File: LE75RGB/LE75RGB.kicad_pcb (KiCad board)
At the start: 2 copper layers, 285 x 94.6 mm, 256 parts, among them P1 USB_C_Plug_USB2.0, SW1 SW_Push, U1 MCP1703Ax-330xxDB, U2 STM32F072CBTx

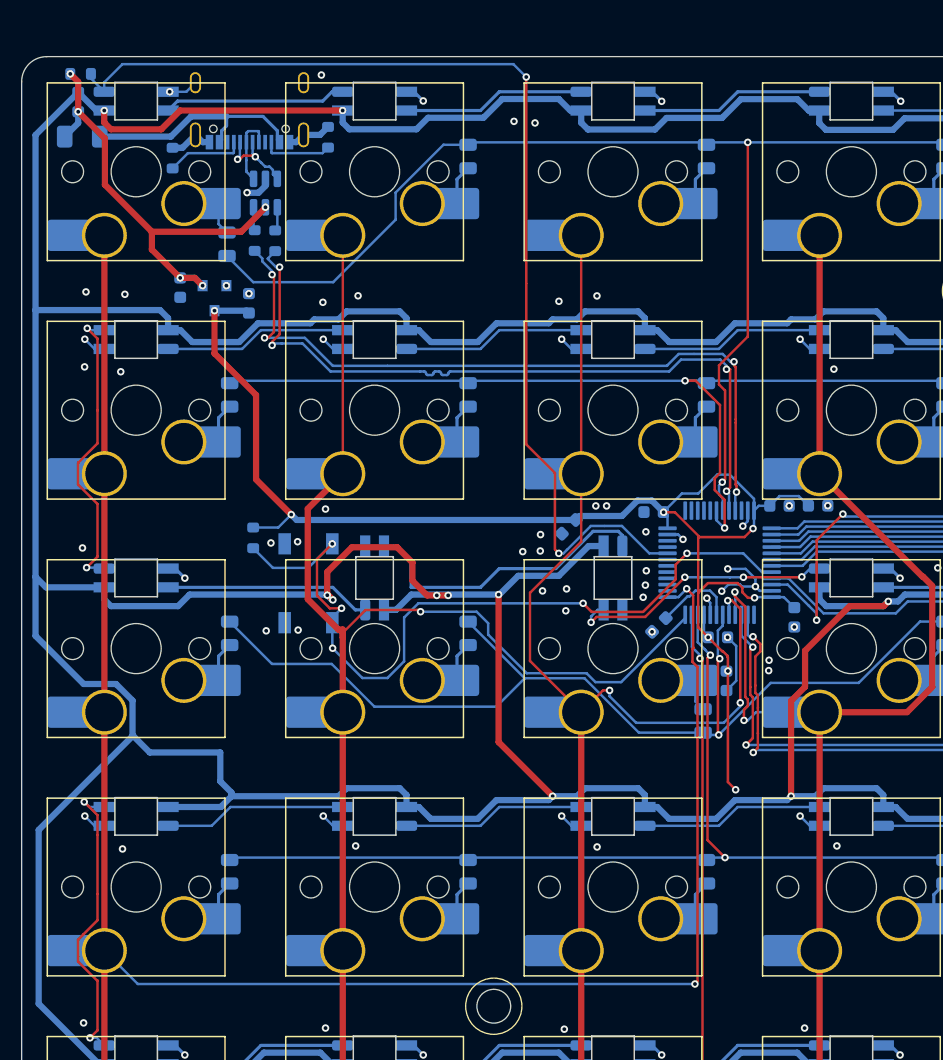
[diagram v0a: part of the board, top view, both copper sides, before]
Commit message: updated RGB variants
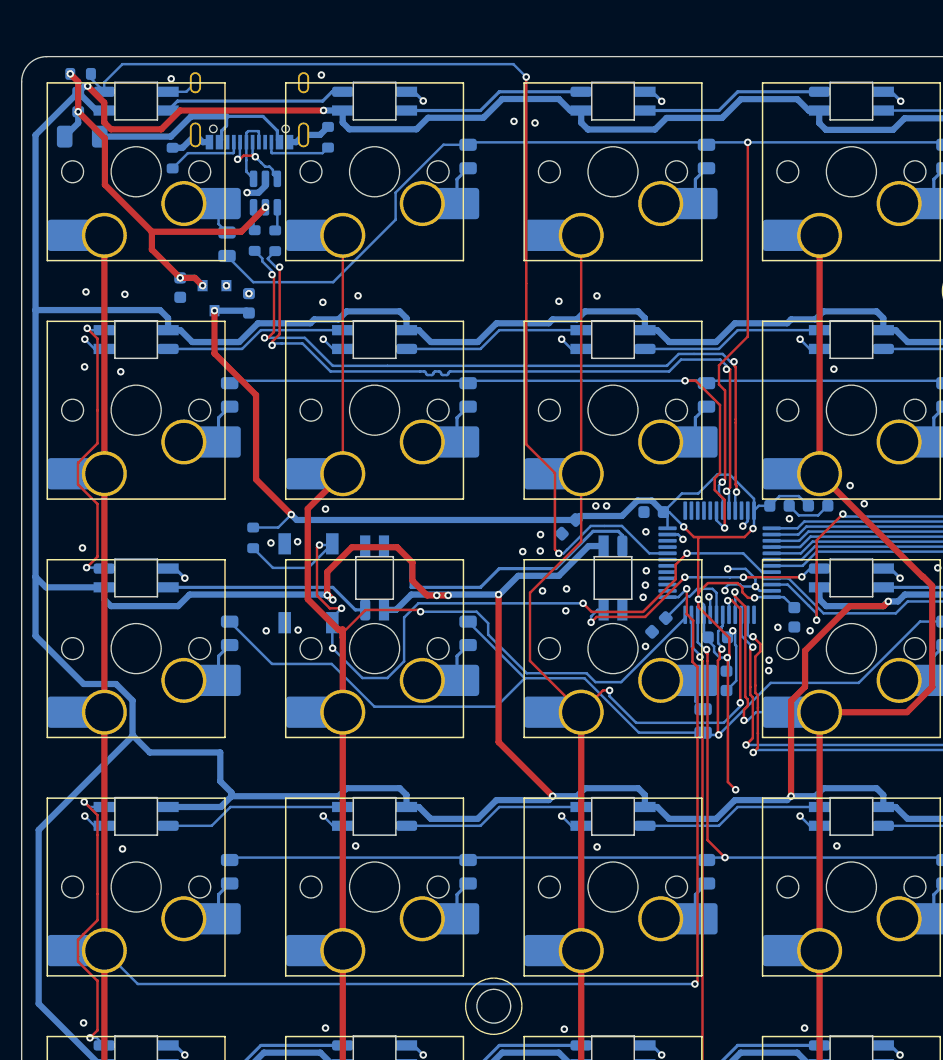
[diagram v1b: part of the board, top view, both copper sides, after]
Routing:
- net VCC: track 115.2 -> 120.4 mm
- net GND: track 153.2 -> 157.2 mm, vias 172 -> 174
- net Net-(D100-VDD): track 1694.3 -> 1697.8 mm
- net Net-(U2-BOOT0): track 62.5 -> 63.0 mm
